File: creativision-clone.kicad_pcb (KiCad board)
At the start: 2 copper layers, 107 parts, among them J1 Conn_01x10_Socket, J2 Conn_01x10_Socket, J3 Conn_01x07_Pin, J4 Conn_01x04_Socket, J5 RCJ-013, J6 RCJ-014, Q1 2n4401, SW1 Reset, SW2 Power Toggle, U1 AS6C62256-DIP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

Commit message: Enough for one night
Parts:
- removed C10, C106, C11: 100µF, Capacitor_THT:CP_Radial_D6.3mm_P2.50mm
- removed JP1, JP2, JP3, JP4: SolderJumper_2_Bridged, Jumper:SolderJumper-2_P1.3mm_Bridged2Bar_RoundedPad1.0x1.5mm
- moved C2 254.5 mm to (268.9, 128.7), turned to 90 degrees
- moved R4 243.9 mm to (259.3, 58.8)
- moved U3 236.4 mm to (227.3, 111.8), turned to 180 degrees
- moved J5 232.3 mm to (258.6, 44.6), turned to -90 degrees
- moved R5 226.9 mm to (222.3, 118.0), turned to 180 degrees
- moved Q1 206.5 mm to (249.2, 46.8), turned to 180 degrees
- moved C6 205.7 mm to (252.4, 59.5)
- moved J6 205.1 mm to (220.0, 44.6), turned to -90 degrees
- moved R3 201.3 mm to (214.9, 58.2)
- moved R14 193.5 mm to (181.6, 129.5), turned to 90 degrees
- moved C9 191.0 mm to (206.2, 120.5), turned to 90 degrees
- moved U99 188.4 mm to (260.9, 64.0)
- moved C8 178.3 mm to (206.2, 99.5), turned to -90 degrees
- moved C14 177.4 mm to (199.1, 112.8)
- moved R27 176.2 mm to (196.3, 50.2), turned to 180 degrees
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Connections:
- net Net-(C13-Pad2) renamed /SW_VCC
- U20 pad 2: Net-(JP2-B) -> GND
- U20 pad 23: Net-(JP1-B) -> GND
- U20 pad 26: Net-(JP3-B) -> GND
- U20 pad 27: Net-(JP4-B) -> GND
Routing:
- net /~{RESET}: track 0.00 -> 181.1 mm, vias 0 -> 6
- net Net-(U2-~{NMI}): track 0.00 -> 149.7 mm, vias 0 -> 3
- net GND: track 0.00 -> 147.7 mm, vias 0 -> 8
- net /~{WRAM_WE}: track 0.00 -> 139.9 mm, vias 0 -> 4
- net /R/~{W}: track 0.00 -> 136.2 mm, vias 0 -> 7
- net Net-(D16-A): track 25.7 -> 152.9 mm, vias 0 -> 4
- net /~{WRAM_OE}: track 0.00 -> 124.1 mm, vias 0 -> 4
- net /AUDIO_IN: track 0.00 -> 122.7 mm, vias 0 -> 1
- net /~{PIA}: track 0.00 -> 121.3 mm, vias 0 -> 2
- net Net-(D15-A): track 25.7 -> 136.6 mm, vias 0 -> 4
- net /a14: track 0.00 -> 110.1 mm, vias 0 -> 4
- net /VDP_W~{R}: track 0.00 -> 108.1 mm, vias 0 -> 4
- net /vd7: track 0.00 -> 106.7 mm, vias 0 -> 4
- net /ad7: track 0.00 -> 105.6 mm, vias 0 -> 5
- net /VDP_R~{W}: track 0.00 -> 105.4 mm, vias 0 -> 6
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- added copper zone on F.Cu, net +5V
- added copper zone on B.Cu, net GND
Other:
- board outline added: 205.7 x 99.7 mm
- board text added: "+12V"
- board text added: "+5V"
- board text added: "+9V"
- board text added: "-5V"
- board text added: "Audio In"
- board text added: "E"
- board text added: "Expansion Power (Opt.)"
- board text added: "GND"
- board text added: "N/C"
- board text added: "RAM A11"
- board text added: "TAPE_VCC"
- board text added: "TODO: name the other pins in human language"

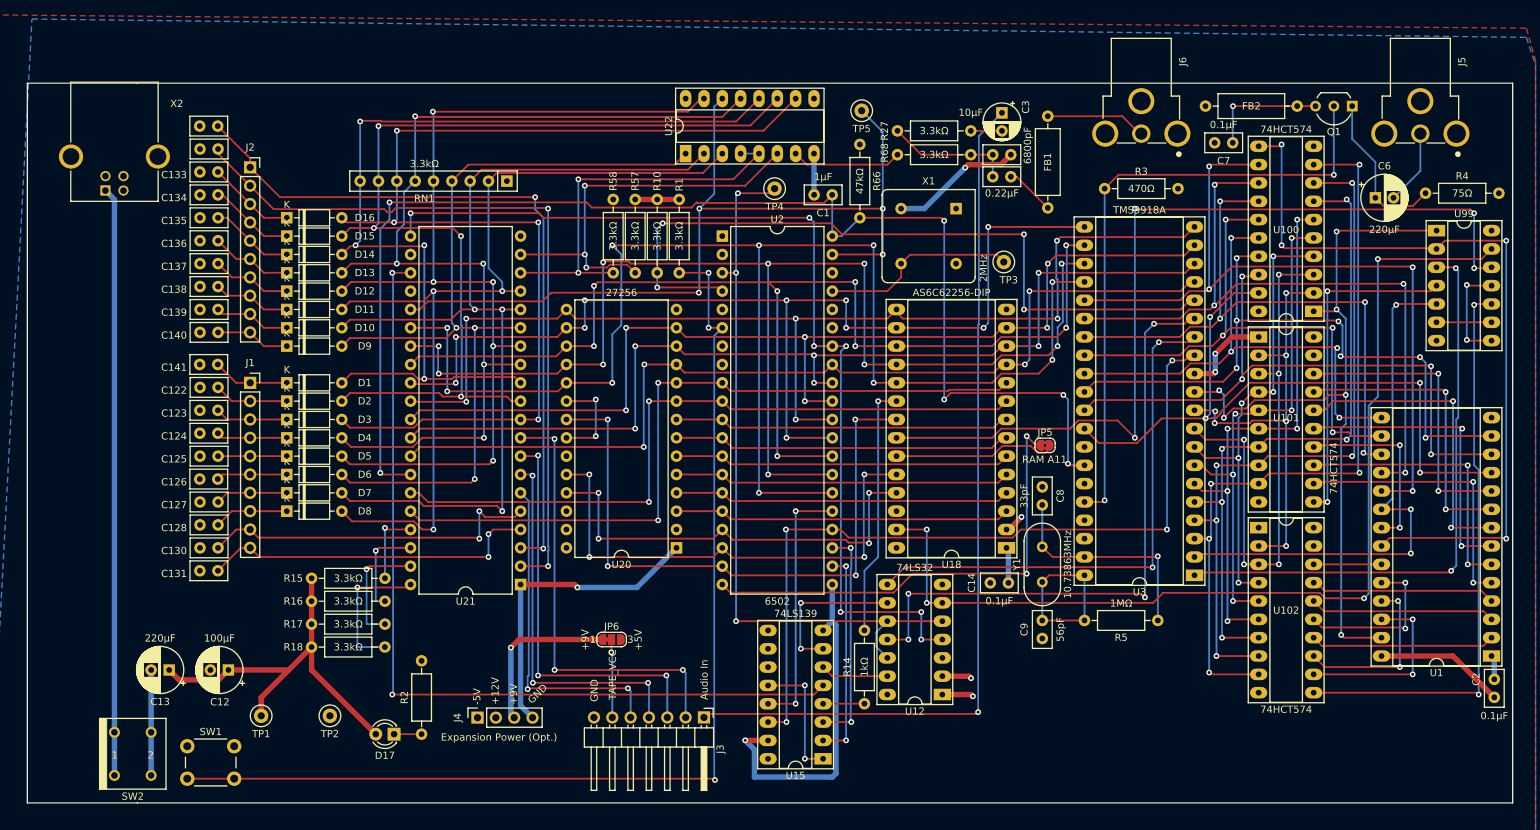
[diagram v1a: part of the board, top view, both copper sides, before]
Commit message: Mounting holes
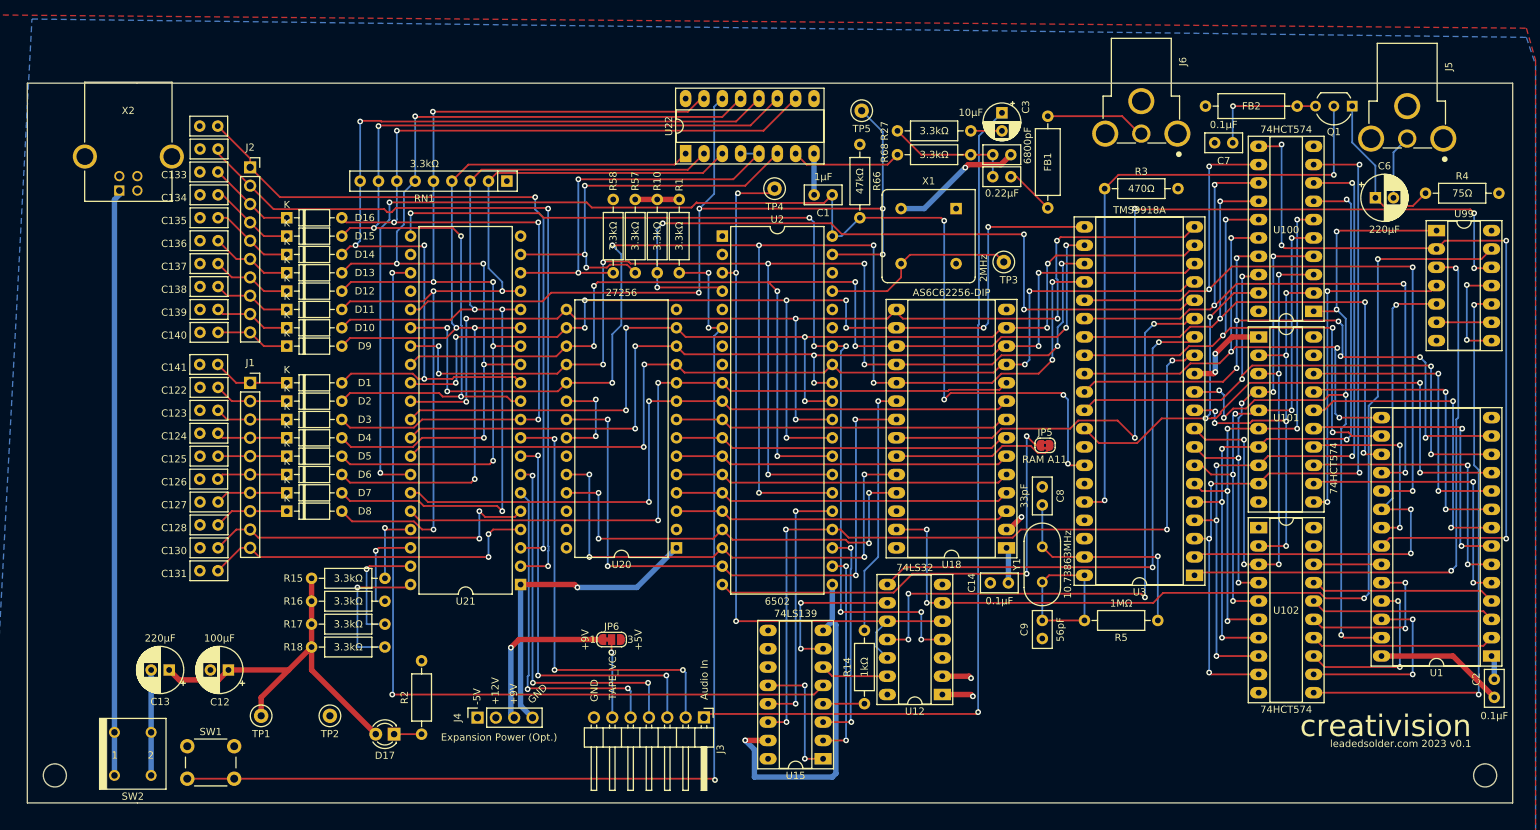
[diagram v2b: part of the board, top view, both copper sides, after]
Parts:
- added REF**: MountingHole_3.2mm_M3, MountingHole:MountingHole_3.2mm_M3, F.Cu at (267.6, 139.5)
- added REF**: MountingHole_3.2mm_M3, MountingHole:MountingHole_3.2mm_M3, F.Cu at (69.5, 139.5)
- moved J5 1.95 mm to (256.8, 45.3)
- moved X2 1.93 mm to (79.7, 53.7)
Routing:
- net Net-(C6-Pad2): track 10.4 -> 8.99 mm
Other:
- board text added: "creativision"
- board text added: "leadedsolder.com 2023 v0.1"
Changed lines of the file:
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@@
     )
   )
+  (footprint "MountingHole:MountingHole_3.2mm_M3" locked (layer "F.Cu")
+    (at 267.59 139.472929)
+    (descr "Mounting Hole 3.2mm, no annular, M3")
+    (tags "mounting hole 3.2mm no annular m3")
+    (attr exclude_from_pos_files exclude_from_bom)
+    (fp_text reference "REF**" (at 0 -4.2) (layer "F.SilkS") hide
+        (effects (font (size 1 1) (thickness 0.15)))
+    )
+    (fp_text value "MountingHole_3.2mm_M3" (at 0 4.2) (layer "F.Fab")
+        (effects (font (size 1 1) (thickness 0.15)))
+    )
+    (fp_text user "${REFERENCE}" (at 0 0) (layer "F.Fab")
+        (effects (font (size 1 1) (thickness 0.15)))
+    )
+    (fp_circle (center 0 0) (end 3.2 0)
+      (stroke (width 0.15) (type solid)) (fill none) (layer "Cmts.User"))
+    (fp_circle (center 0 0) (end 3.45 0)
+      (stroke (width 0.05) (type solid)) (fill none) (layer "F.CrtYd"))
+    (pad "" np_thru_hole circle locked (at 0 0) (size 3.2 3.2) (drill 3.2) (layers "*.Cu" "*.Mask"))
+  )
   (footprint "Capacitor_THT:CP_Radial_D6.3mm_P2.50mm" (layer "F.Cu")
     (at 85.305 124.867929 180)
@@
   )
   (footprint "USB-B1HSB6:OST_USB-B1HSB6" (layer "F.Cu")
-    (at 77.725 53.747929 180)
+    (at 79.65 53.747929 180)
     (property "DigiKey" "ED2983-ND\r")
     (property "MANUFACTURER" "ON-SHORE TECHNOLOGY")
@@
     (property "Sheetname" "")
     (attr through_hole)
-    (fp_text reference "X2" (at -8.638335 7.327875) (layer "F.SilkS")
+    (fp_text reference "X2" (at 0.02 6.35) (layer "F.SilkS")
         (effects (font (size 1.000386 1.000386) (thickness 0.15)))
     )
@@
   )
   (footprint "Jacks:CUI_RCJ-017" (layer "F.Cu")
-    (at 258.62 44.622929 -90)
+    (at 256.795 45.312929 -90)
     (descr "<b>DC POWER JACK</b><p>Source: DCJ0202.pdf")
     (property "Digi-Key" "Manufacturer recommendations")
@@
     )
   )
+  (footprint "MountingHole:MountingHole_3.2mm_M3" locked (layer "F.Cu")
+    (at 69.47 139.472929)
+    (descr "Mounting Hole 3.2mm, no annular, M3")
+    (tags "mounting hole 3.2mm no annular m3")
+    (attr exclude_from_pos_files exclude_from_bom)
+    (fp_text reference "REF**" (at 0 -4.2) (layer "F.SilkS") hide
+        (effects (font (size 1 1) (thickness 0.15)))
+    )
+    (fp_text value "MountingHole_3.2mm_M3" (at 0 4.2) (layer "F.Fab")
+        (effects (font (size 1 1) (thickness 0.15)))
+    )
+    (fp_text user "${REFERENCE}" (at 0 0) (layer "F.Fab")
+        (effects (font (size 1 1) (thickness 0.15)))
+    )
+    (fp_circle (center 0 0) (end 3.2 0)
+      (stroke (width 0.15) (type solid)) (fill none) (layer "Cmts.User"))
+    (fp_circle (center 0 0) (end 3.45 0)
+      (stroke (width 0.05) (type solid)) (fill none) (layer "F.CrtYd"))
+    (pad "" np_thru_hole circle locked (at 0 0) (size 3.2 3.2) (drill 3.2) (layers "*.Cu" "*.Mask"))
+    (pad "" np_thru_hole circle locked (at 0 0) (size 3.2 3.2) (drill 3.2) (layers "*.Cu" "*.Mask"))
+    (pad "" np_thru_hole circle locked (at 0 0) (size 3.2 3.2) (drill 3.2) (layers "*.Cu" "*.Mask"))
+  )
   (footprint "Capacitor_THT:C_Disc_D5.0mm_W2.5mm_P2.50mm" (layer "F.Cu")
     (at 92.055 88.9 180)
@@
     (effects (font (size 1 1) (thickness 0.15)) (justify left bottom))
   )
+  (gr_text "leadedsolder.com 2023 v0.1" (at 265.685 135.662929) (layer "F.SilkS")
+    (effects (font (size 1 1) (thickness 0.15)) (justify right bottom))
+  )
   (gr_text "RAM A11" (at 203.455 96.292929) (layer "F.SilkS")
     (effects (font (size 1 1) (thickness 0.15)) (justify left bottom))
@@
     (effects (font (size 1 1) (thickness 0.15)) (justify left bottom))
   )
+  (gr_text "creativision" (at 265.685 134.392929) (layer "F.SilkS")
+    (effects (font (size 3 3) (thickness 0.15)) (justify right bottom))
+  )
   (gr_text "GND" (at 135.637 129.693929 45) (layer "F.SilkS")
     (effects (font (size 1 1) (thickness 0.15)) (justify left bottom))
@@
   (segment (start 259.335 58.827929) (end 257.575 60.587929) (width 0.25) (layer "F.Cu") (net 8))
   (segment (start 253.515 60.587929) (end 252.39 59.462929) (width 0.25) (layer "F.Cu") (net 8))
-  (segment (start 249.175 46.762929) (end 249.175 51.296653) (width 0.25) (layer "B.Cu") (net 8))
-  (segment (start 249.175 51.296653) (end 252.39 54.511653) (width 0.25) (layer "B.Cu") (net 8))
-  (segment (start 252.39 54.511653) (end 252.39 59.462929) (width 0.25) (layer "B.Cu") (net 8))
-  (segment (start 258.62 50.572929) (end 258.62 55.732929) (width 0.25) (layer "B.Cu") (net 9))
-  (segment (start 258.62 55.732929) (end 254.89 59.462929) (width 0.25) (layer "B.Cu") (net 9))
+  (segment (start 252.39 55.017929) (end 252.39 59.462929) (width 0.25) (layer "B.Cu") (net 8))
+  (segment (start 249.175 51.802929) (end 252.39 55.017929) (width 0.25) (layer "B.Cu") (net 8))
+  (segment (start 249.175 46.762929) (end 249.175 51.802929) (width 0.25) (layer "B.Cu") (net 8))
+  (segment (start 256.795 51.262929) (end 254.89 53.167929) (width 0.25) (layer "B.Cu") (net 9))
+  (segment (start 254.89 53.167929) (end 254.89 59.462929) (width 0.25) (layer "B.Cu") (net 9))
   (segment (start 244.095 46.762929) (end 241.555 46.762929) (width 0.25) (layer "F.Cu") (net 10))
   (segment (start 241.555 46.762929) (end 232.665 46.762929) (width 0.25) (layer "F.Cu") (net 10))
@@
   (segment (start 173.61 54.865) (end 184.811929 54.865) (width 0.25) (layer "F.Cu") (net 64))
   (segment (start 184.811929 54.865) (end 186.183 53.493929) (width 0.25) (layer "F.Cu") (net 64))
+  (segment (start 78.4 58.457929) (end 78.4 59.032929) (width 0.75) (layer "B.Cu") (net 65))
   (segment (start 77.725 133.503929) (end 77.725 59.707929) (width 0.75) (layer "B.Cu") (net 65))
   (segment (start 77.725 139.472929) (end 77.725 133.503929) (width 0.75) (layer "B.Cu") (net 65))
-  (segment (start 77.725 59.707929) (end 76.475 58.457929) (width 0.75) (layer "B.Cu") (net 65))
+  (segment (start 78.4 59.032929) (end 77.725 59.707929) (width 0.75) (layer "B.Cu") (net 65))
   (segment (start 184.785 72.39) (end 177.165 72.39) (width 0.25) (layer "F.Cu") (net 66))
   (segment (start 187.917071 67.352929) (end 186.69 68.58) (width 0.25) (layer "F.Cu") (net 66))

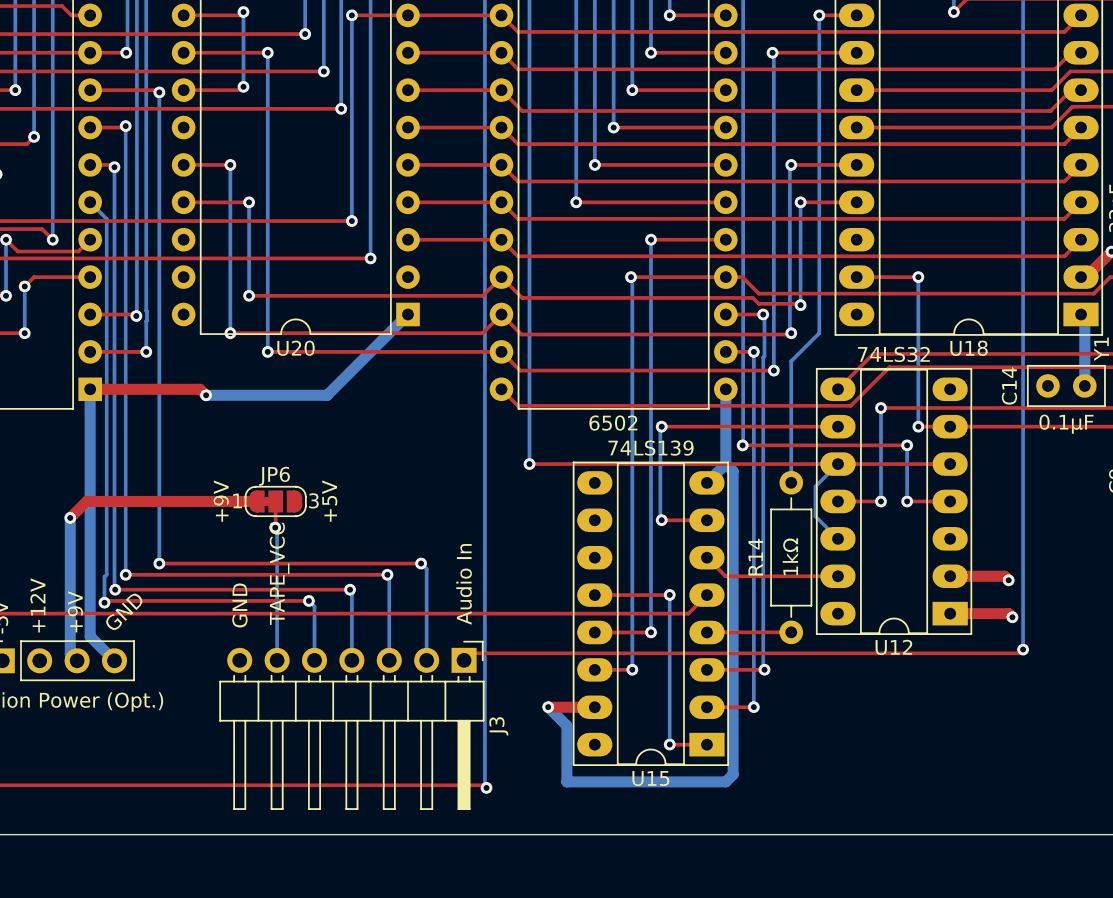
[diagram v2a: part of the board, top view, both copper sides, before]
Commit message: Fix backwards tape header
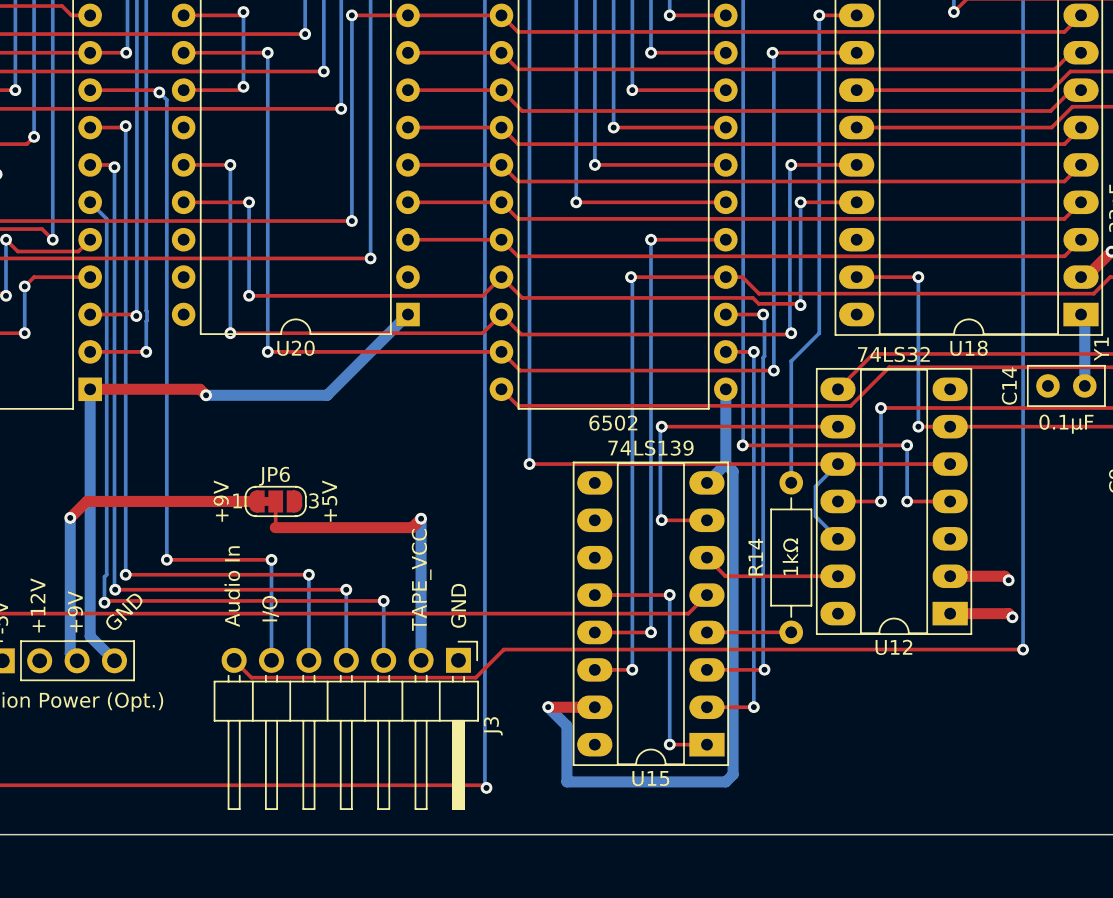
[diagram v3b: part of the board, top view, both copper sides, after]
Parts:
- moved J3 0.38 mm to (159.0, 131.4)
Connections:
- J3 pad 1: /AUDIO_IN -> GND
- J3 pad 2: /PA7 -> /TAPE_VCC
- J3 pad 3: /PA6 -> /PA4
- J3 pad 5: /PA4 -> /PA6
- J3 pad 6: /TAPE_VCC -> /PA7
- J3 pad 7: GND -> /AUDIO_IN
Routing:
- net /AUDIO_IN: track 122.7 -> 139.3 mm
- net /TAPE_VCC: track 10.9 -> 21.6 mm
- net /PA7: track 61.3 -> 50.7 mm
- net /PA6: track 56.6 -> 51.2 mm
- net /PA4: track 45.9 -> 50.8 mm
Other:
- board text added: "I/O"
- board text removed: "TODO: name the other pins in human language"
